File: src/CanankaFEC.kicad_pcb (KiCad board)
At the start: 2 copper layers, 24 x 27.9 mm, 27 parts, among them J1 B3B-XH-A, P1 105444-0001, U1 FT232RL, U2 PIC18F25K80

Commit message: Moved TVS to bottom
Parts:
- D1: moved to B.Cu
- moved D1 3.60 mm to (32.0, 40.4), turned to 180 degrees
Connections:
- D1 pad 1: CANL -> CANH
- D1 pad 2: CANH -> CANL
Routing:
- net CANH: track 16.3 -> 19.9 mm, vias 1 -> 2
- net GND: track 115.1 -> 116.9 mm
- net 5V_SW: track 63.4 -> 62.5 mm
- net CANL: track 13.2 -> 12.4 mm, vias 1 -> 2

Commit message: Swapped UART lines
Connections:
- U2 pad 17: TXD -> RXD
- U2 pad 18: RXD -> TXD
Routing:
- net TXD: track 15.6 -> 19.4 mm
- net TERMINATE: track 9.98 -> 12.6 mm, vias 1 -> 2
- net RXD: track 17.5 -> 19.6 mm
- net LED_ACTIVITY: track 15.2 -> 16.9 mm, vias 1 -> 3
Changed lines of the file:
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@@
       (net 22 "LED_ACTIVITY") (thermal_bridge_angle 45))
     (pad "17" smd roundrect (at 3.5 2.925) (size 1.75 0.45) (layers "F.Cu" "F.Paste" "F.Mask") (roundrect_rratio 0.25)
+      (net 4 "RXD") (thermal_bridge_angle 45))
+    (pad "18" smd roundrect (at 3.5 2.275) (size 1.75 0.45) (layers "F.Cu" "F.Paste" "F.Mask") (roundrect_rratio 0.25)
       (net 2 "TXD") (thermal_bridge_angle 45))
-    (pad "18" smd roundrect (at 3.5 2.275) (size 1.75 0.45) (layers "F.Cu" "F.Paste" "F.Mask") (roundrect_rratio 0.25)
-      (net 4 "RXD") (thermal_bridge_angle 45))
     (pad "19" smd roundrect (at 3.5 1.625) (size 1.75 0.45) (layers "F.Cu" "F.Paste" "F.Mask") (roundrect_rratio 0.25)
       (net 7 "GND") (thermal_bridge_angle 45))
@@
   (via (at 21.9 23.8) (size 0.6) (drill 0.3) (layers "F.Cu" "B.Cu") (net 1))
   (segment (start 21.9 23.8) (end 21.9 26.13) (width 0.2) (layer "B.Cu") (net 1))
-  (segment (start 40.711396 32.925) (end 41.9 32.925) (width 0.3) (layer "F.Cu") (net 2))
+  (segment (start 32.102818 34.225) (end 33.677818 35.8) (width 0.3) (layer "F.Cu") (net 2))
+  (segment (start 43.55 34.95) (end 43.55 32.9) (width 0.3) (layer "F.Cu") (net 2))
+  (segment (start 43.55 32.9) (end 42.925 32.275) (width 0.3) (layer "F.Cu") (net 2))
   (segment (start 33.677818 35.8) (end 39.5 35.8) (width 0.3) (layer "F.Cu") (net 2))
-  (segment (start 40.4 33.236396) (end 40.711396 32.925) (width 0.3) (layer "F.Cu") (net 2))
-  (segment (start 32.102818 34.225) (end 33.677818 35.8) (width 0.3) (layer "F.Cu") (net 2))
-  (segment (start 40.4 34.9) (end 40.4 33.236396) (width 0.3) (layer "F.Cu") (net 2))
-  (segment (start 39.5 35.8) (end 40.4 34.9) (width 0.3) (layer "F.Cu") (net 2))
+  (segment (start 42.925 32.275) (end 41.9 32.275) (width 0.3) (layer "F.Cu") (net 2))
   (segment (start 29.1 34.225) (end 32.102818 34.225) (width 0.3) (layer "F.Cu") (net 2))
+  (segment (start 39.5 35.8) (end 39.55 35.75) (width 0.3) (layer "F.Cu") (net 2))
+  (segment (start 39.55 35.75) (end 42.75 35.75) (width 0.3) (layer "F.Cu") (net 2))
+  (segment (start 42.75 35.75) (end 43.55 34.95) (width 0.3) (layer "F.Cu") (net 2))
   (segment (start 23.775 29.025) (end 24.15 29.4) (width 0.2) (layer "F.Cu") (net 3))
   (segment (start 28.047793 32.275) (end 29.1 32.275) (width 0.2) (layer "F.Cu") (net 3))
@@
   (segment (start 26 30.1) (end 27.0495 30.1) (width 0.2) (layer "B.Cu") (net 3))
   (segment (start 26 32.9) (end 23.6 32.9) (width 0.2) (layer "B.Cu") (net 3))
-  (segment (start 40.625 32.275) (end 41.9 32.275) (width 0.3) (layer "F.Cu") (net 4))
+  (segment (start 30.5 33.55) (end 30.65 33.7) (width 0.3) (layer "F.Cu") (net 4))
   (segment (start 29.1 31.625) (end 30.225 31.625) (width 0.3) (layer "F.Cu") (net 4))
-  (segment (start 39.9 34.7) (end 39.9 33) (width 0.3) (layer "F.Cu") (net 4))
-  (segment (start 30.5 33.55) (end 30.65 33.7) (width 0.3) (layer "F.Cu") (net 4))
-  (segment (start 39.3 35.3) (end 39.9 34.7) (width 0.3) (layer "F.Cu") (net 4))
+  (segment (start 43.1 34.763604) (end 43.1 33.15) (width 0.3) (layer "F.Cu") (net 4))
   (segment (start 30.65 33.7) (end 32.3 33.7) (width 0.3) (layer "F.Cu") (net 4))
-  (segment (start 33.9 35.3) (end 39.3 35.3) (width 0.3) (layer "F.Cu") (net 4))
-  (segment (start 39.9 33) (end 40.625 32.275) (width 0.3) (layer "F.Cu") (net 4))
+  (segment (start 42.563604 35.3) (end 43.1 34.763604) (width 0.3) (layer "F.Cu") (net 4))
+  (segment (start 30.5 31.9) (end 30.5 33.55) (width 0.3) (layer "F.Cu") (net 4))
+  (segment (start 33.9 35.3) (end 42.563604 35.3) (width 0.3) (layer "F.Cu") (net 4))
+  (segment (start 32.3 33.7) (end 33.9 35.3) (width 0.3) (layer "F.Cu") (net 4))
   (segment (start 30.225 31.625) (end 30.5 31.9) (width 0.3) (layer "F.Cu") (net 4))
-  (segment (start 30.5 31.9) (end 30.5 33.55) (width 0.3) (layer "F.Cu") (net 4))
-  (segment (start 32.3 33.7) (end 33.9 35.3) (width 0.3) (layer "F.Cu") (net 4))
+  (segment (start 43.1 33.15) (end 42.875 32.925) (width 0.3) (layer "F.Cu") (net 4))
+  (segment (start 42.875 32.925) (end 41.9 32.925) (width 0.3) (layer "F.Cu") (net 4))
   (segment (start 22.1 25.775) (end 23.517894 25.775) (width 0.35) (layer "F.Cu") (net 5))
   (segment (start 31.75 23.15) (end 31.75 22.1) (width 0.35) (layer "F.Cu") (net 5))
@@
   (segment (start 22.7 46.3) (end 21.2 44.8) (width 0.2) (layer "B.Cu") (net 20))
   (segment (start 24.5 46.5) (end 24.5 44.15) (width 0.2) (layer "B.Cu") (net 21))
-  (segment (start 40.4 38.701103) (end 43.3 35.801103) (width 0.2) (layer "F.Cu") (net 22))
-  (segment (start 42.975 33.575) (end 41.9 33.575) (width 0.2) (layer "F.Cu") (net 22))
-  (segment (start 40.4 45.05) (end 40.4 38.701103) (width 0.2) (layer "F.Cu") (net 22))
-  (segment (start 39.85 45.6) (end 40.4 45.05) (width 0.2) (layer "F.Cu") (net 22))
-  (segment (start 43.3 33.9) (end 42.975 33.575) (width 0.2) (layer "F.Cu") (net 22))
-  (segment (start 43.3 35.801103) (end 43.3 33.9) (width 0.2) (layer "F.Cu") (net 22))
+  (segment (start 40.974984 33.575) (end 40.5 33.100016) (width 0.2) (layer "F.Cu") (net 22))
+  (segment (start 42.65 36.45) (end 42.65 36.35) (width 0.2) (layer "F.Cu") (net 22))
+  (segment (start 41.9 33.575) (end 40.974984 33.575) (width 0.2) (layer "F.Cu") (net 22))
+  (segment (start 39.85 39.25) (end 42.65 36.45) (width 0.2) (layer "F.Cu") (net 22))
+  (segment (start 39.85 45.6) (end 39.85 39.25) (width 0.2) (layer "F.Cu") (net 22))
+  (via (at 42.65 36.35) (size 0.6) (drill 0.3) (layers "F.Cu" "B.Cu") (net 22))
   (via (at 39.85 45.65) (size 0.6) (drill 0.3) (layers "F.Cu" "B.Cu") (net 22))
+  (via (at 40.5 33.100016) (size 0.6) (drill 0.3) (layers "F.Cu" "B.Cu") (net 22))
   (segment (start 39.85 46.15) (end 39.85 45.65) (width 0.2) (layer "B.Cu") (net 22))
-  (segment (start 41.9 36.3) (end 41.9 34.225) (width 0.2) (layer "F.Cu") (net 23))
-  (via (at 41.9 36.3) (size 0.6) (drill 0.3) (layers "F.Cu" "B.Cu") (net 23))
-  (segment (start 39.05 36.8) (end 41.4 36.8) (width 0.2) (layer "B.Cu") (net 23))
-  (segment (start 41.4 36.8) (end 41.9 36.3) (width 0.2) (layer "B.Cu") (net 23))
+  (segment (start 42.35 34.45) (end 41.000016 33.100016) (width 0.2) (layer "B.Cu") (net 22))
+  (segment (start 42.65 36.35) (end 42.35 36.05) (width 0.2) (layer "B.Cu") (net 22))
+  (segment (start 42.35 36.05) (end 42.35 34.45) (width 0.2) (layer "B.Cu") (net 22))
+  (segment (start 41.000016 33.100016) (end 40.5 33.100016) (width 0.2) (layer "B.Cu") (net 22))
+  (segment (start 40.525004 34.225) (end 40.5 34.250004) (width 0.2) (layer "F.Cu") (net 23))
+  (segment (start 41.9 34.225) (end 40.525004 34.225) (width 0.2) (layer "F.Cu") (net 23))
+  (via (at 41.892372 36.355085) (size 0.6) (drill 0.3) (layers "F.Cu" "B.Cu") (net 23))
+  (via (at 40.5 34.250004) (size 0.6) (drill 0.3) (layers "F.Cu" "B.Cu") (net 23))
   (segment (start 36.5 36.8) (end 39.05 36.8) (width 0.2) (layer "B.Cu") (net 23))
+  (segment (start 41.892372 34.592372) (end 41.892372 36.355085) (width 0.2) (layer "B.Cu") (net 23))
   (segment (start 39.05 36.8) (end 39.05 35.85) (width 0.2) (layer "B.Cu") (net 23))
+  (segment (start 39.05 36.8) (end 41.447457 36.8) (width 0.2) (layer "B.Cu") (net 23))
+  (segment (start 40.5 34.250004) (end 41.550004 34.250004) (width 0.2) (layer "B.Cu") (net 23))
   (segment (start 35.55 35.85) (end 36.5 36.8) (width 0.2) (layer "B.Cu") (net 23))
+  (segment (start 41.550004 34.250004) (end 41.892372 34.592372) (width 0.2) (layer "B.Cu") (net 23))
+  (segment (start 41.447457 36.8) (end 41.892372 36.355085) (width 0.2) (layer "B.Cu") (net 23))
   (segment (start 35.4 25.275) (end 35.4 24.700006) (width 0.2) (layer "F.Cu") (net 24))
   (segment (start 36.5 33.7) (end 36.5 30.9) (width 0.2) (layer "F.Cu") (net 24))

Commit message: Updated connector designators
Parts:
- renumbered P1 to J1, J1 to J2
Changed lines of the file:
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@@
     (descr "Molex 1054440001")
     (attr smd)
-    (fp_text reference "P1" (at 0 -1.7) (layer "F.SilkS") hide
+    (fp_text reference "J1" (at 0 -1.7) (layer "F.SilkS") hide
         (effects (font (size 0.8 0.6) (thickness 0.15)))
     )
@@
     (descr "JST B4B-XH-A [455-B4B-XH-A-ND]")
     (attr through_hole)
-    (fp_text reference "J1" (at 0 2.9) (layer "F.SilkS")
+    (fp_text reference "J2" (at 0 2.9) (layer "F.SilkS")
         (effects (font (size 0.8 0.6) (thickness 0.15) bold))
     )

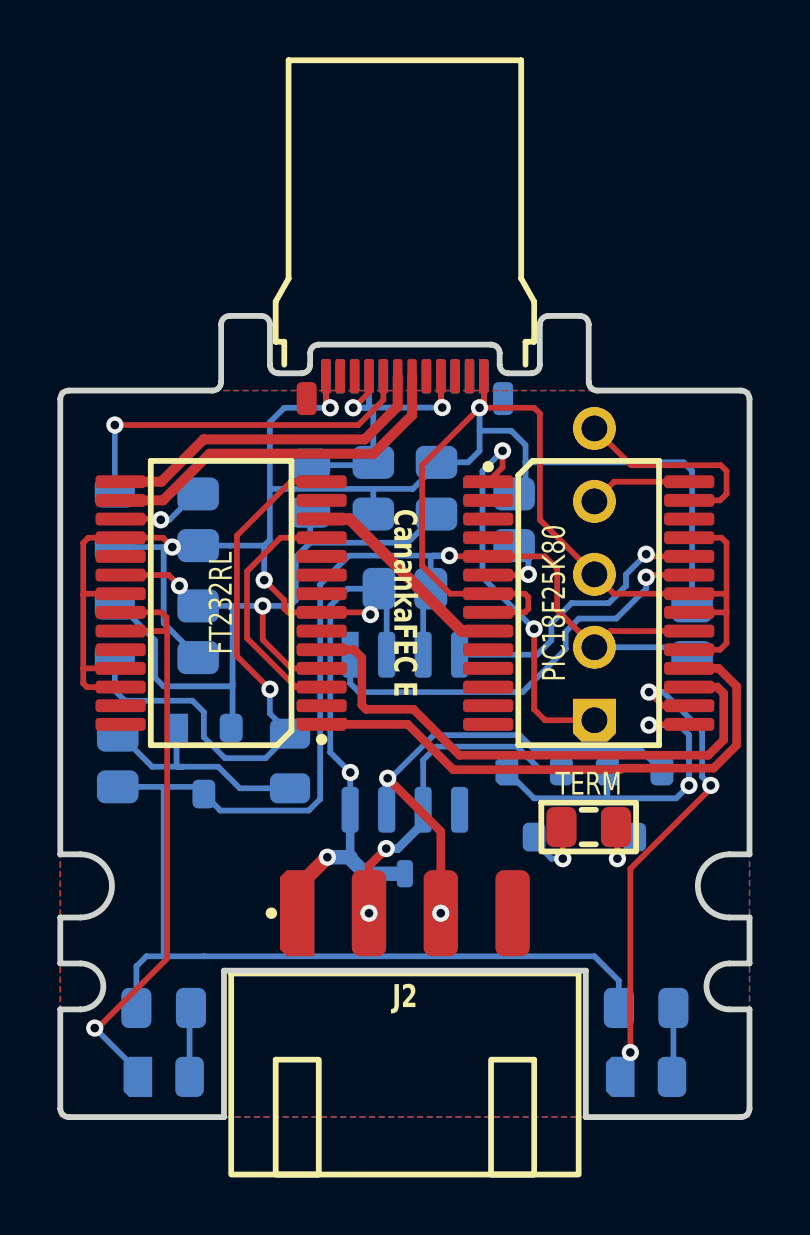
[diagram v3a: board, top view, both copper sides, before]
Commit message: Updated to KiCAD 8
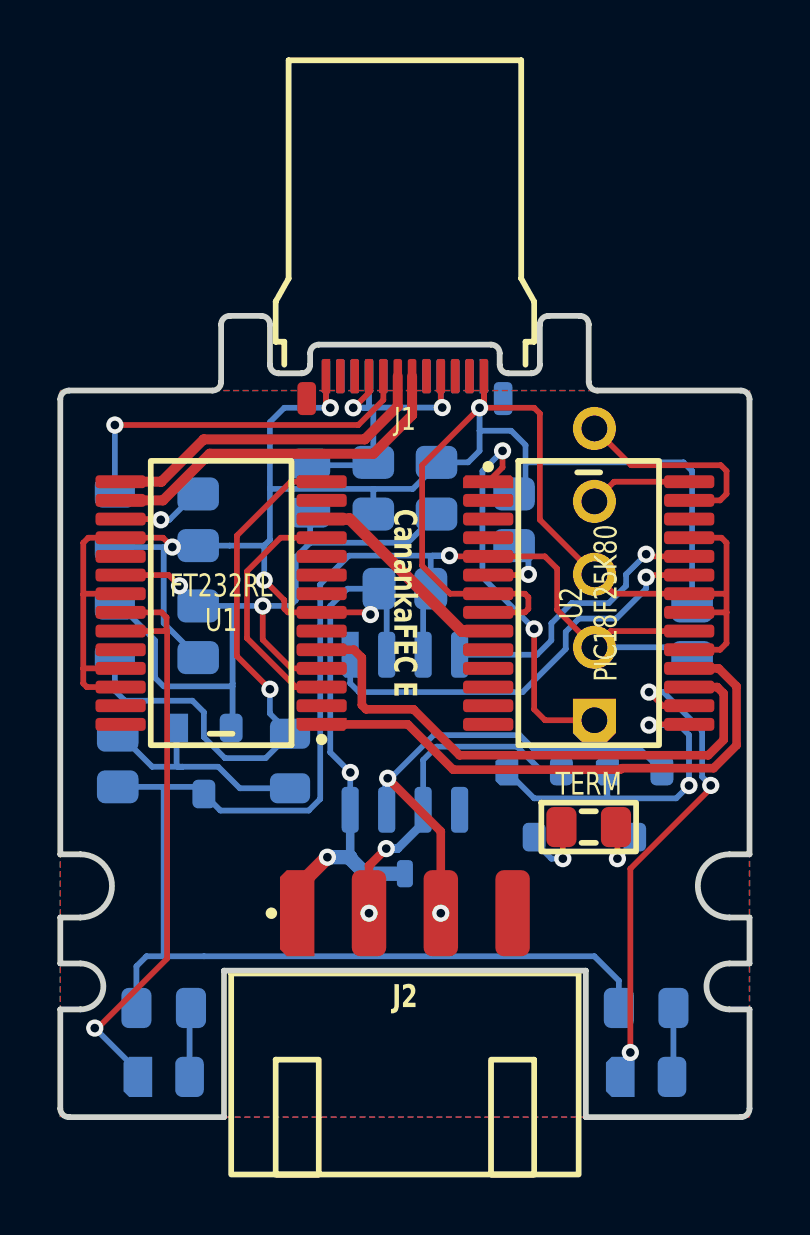
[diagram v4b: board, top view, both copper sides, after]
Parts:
- J1: footprint Medo64:P USB C 3.2 Edge (24w) -> Medo64:J USB C 3.2 Edge (24w)
- U1: footprint Medo64:U Transciever UART FT232RL (SSOP-28) -> Medo64:U Transceiver UART [FT232R] (SSOP-28)
- U2: footprint Medo64:U Micro PIC18F25K80 (SSOP-28) -> Medo64:U Micro [PIC18F25K80] (SSOP-28)
- U?: footprint Medo64:U Transciever CAN MCP2561 (SOIC-8) -> Medo64:U Transceiver CAN [MCP2561] (SOIC-8)

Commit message: Moved termination resistor to bottom
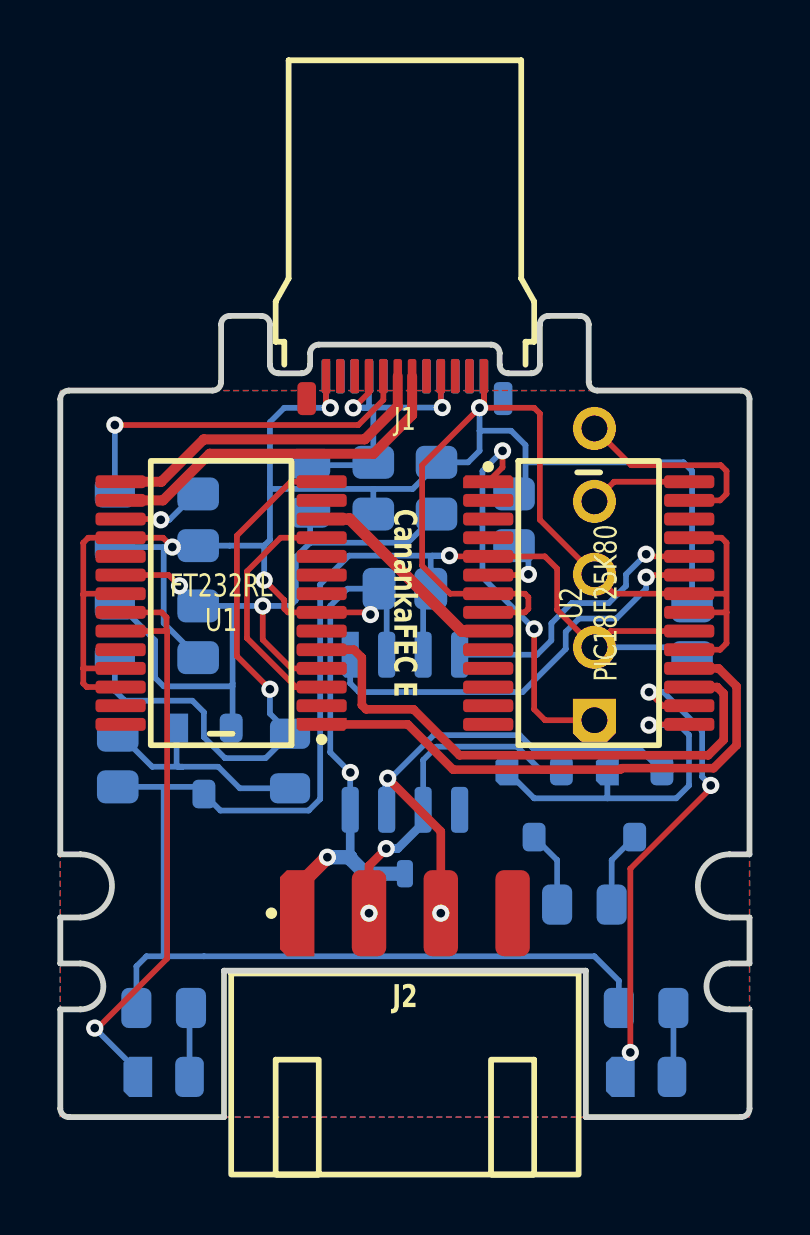
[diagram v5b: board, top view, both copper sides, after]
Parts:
- R1: value TERM -> 118; moved to B.Cu
- moved R1 2.70 mm to (38.2, 40.5)
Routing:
- net GND: track 116.9 -> 116.0 mm
- net CAN_H_TERM: track 1.83 -> 2.68 mm, vias 1 -> 0
- net CANL: track 12.4 -> 11.7 mm
- net CAN_L_TERM: track 1.95 -> 2.68 mm, vias 1 -> 0
- net CANH: track 19.9 -> 19.3 mm
- net TERMINATE: vias 2 -> 1

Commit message: Updated diode footprint
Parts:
- D1: footprint Medo64:D TVS SM05T1G (SOT23-3) -> Medo64:D TVS 24V [PESD24VL2BT,215] (SOT23-3)

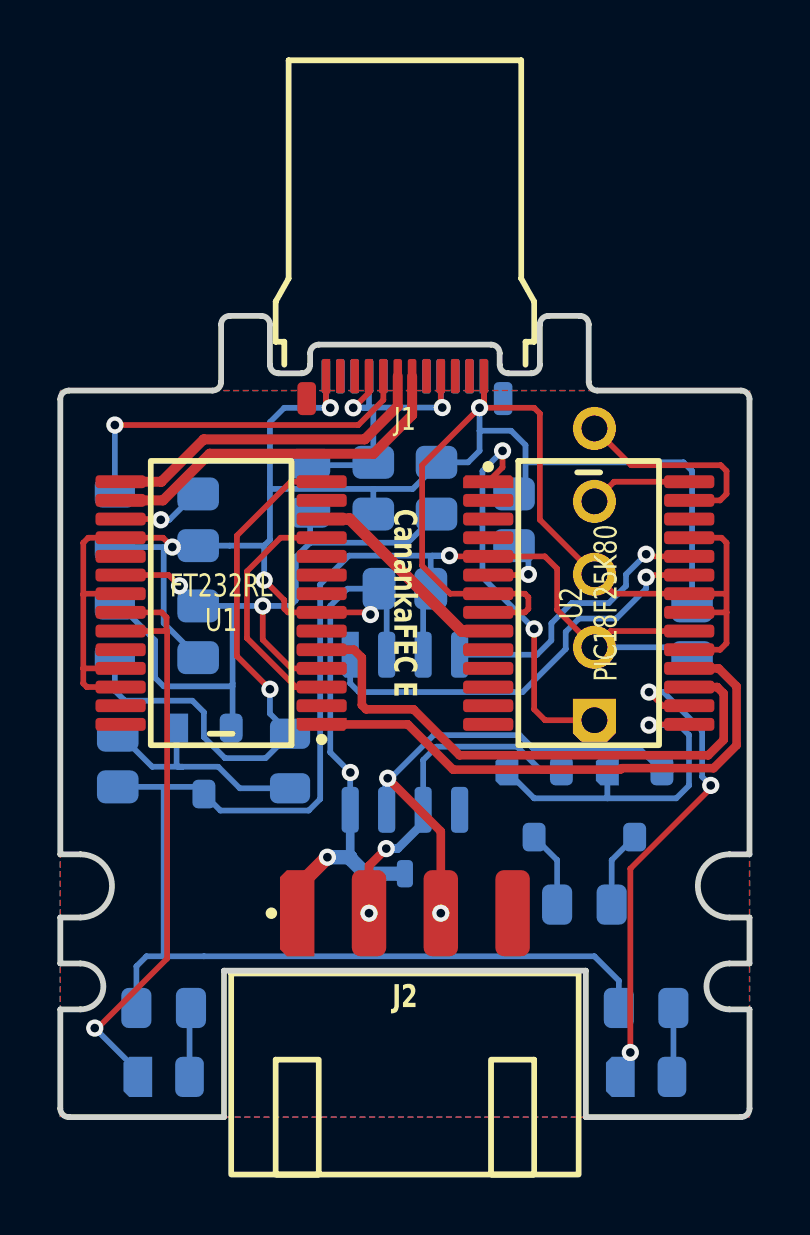
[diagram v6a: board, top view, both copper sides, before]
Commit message: Added board designator
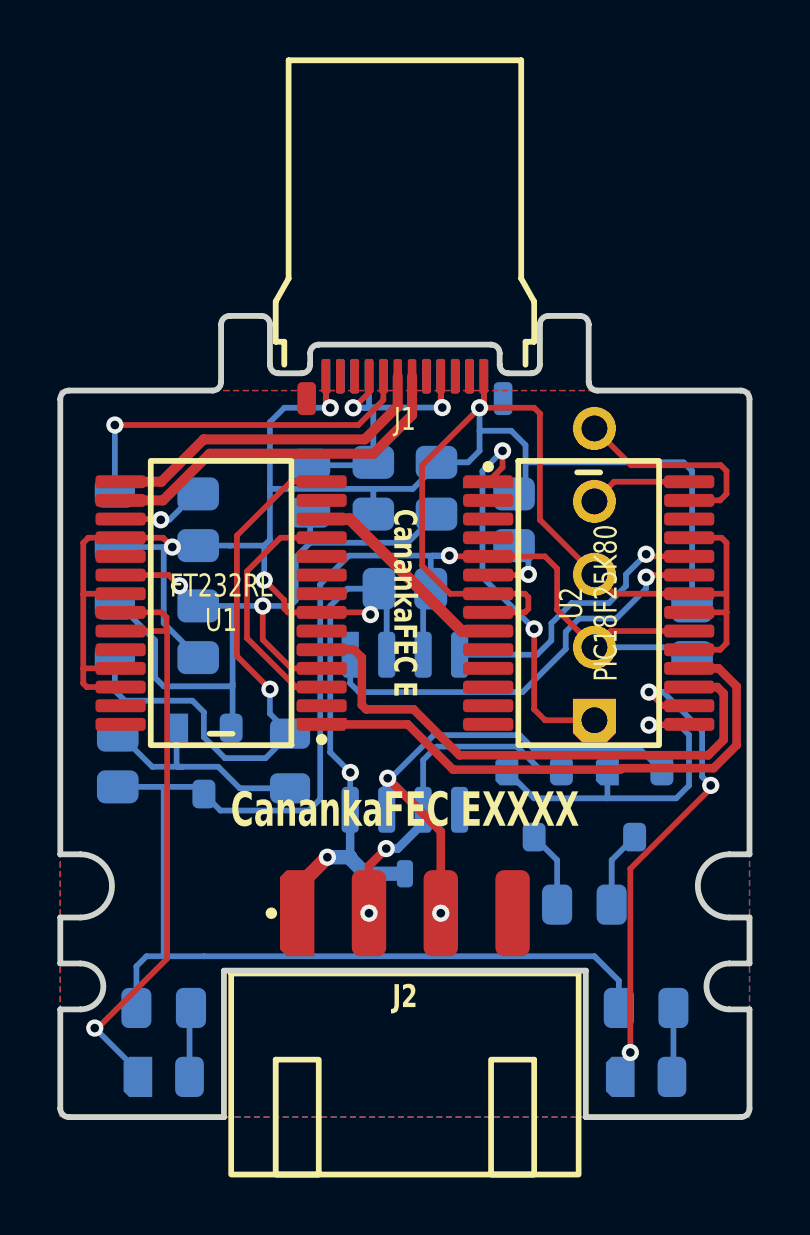
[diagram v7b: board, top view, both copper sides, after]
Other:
- board text added: "CanankaFEC EXXXX"

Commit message: Updated refdes
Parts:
- gave numbers to parts that had none: 1
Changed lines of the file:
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@@
 		(descr "Microchip MCP2561")
 		(tags "SOIC127P600X175-8AN")
-		(property "Reference" "U?"
+		(property "Reference" "U3"
 			(at -0.1 0 0)
 			(layer "B.SilkS")
